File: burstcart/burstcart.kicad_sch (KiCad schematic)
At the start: 17 parts, among them J1 IEC, J2 IEC, J3 BURST, J4 PORTA, U1 27C512, U2 CD74HCT4520E, U3 6526 CIA, U4 20V8, U5 ATtiny85-20P

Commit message: remarks about changes for v1.1
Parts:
- U4: value 20V8 -> 22V10
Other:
- note added: "2-3 normally closed"
- note added: "<- VCC !!! ->"
- note added: "<- remove MUX connection, it's too fast"
- note added: "I've got CD4320 and R1 *must* be shorted, C5 *must* be removed"
- note added: "Phi2 as ciaclk works as well (at least for register r/w) - make it jumperable"
- note added: "ROM_A15 to 22, ~{CIA} to 19 - to make logic possible"
- note added: "SP/CNT are open drain, need 3.3K pullup to VCC"
- note added: "^^^ 22V10"
- note added: "closed = SW delay clock open = HW prescaler clock"
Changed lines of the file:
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@@
+    (effects (font (size 1.27 1.27)) (justify left bottom))
+  )
+  (text "SP/CNT are open drain, need 3.3K pullup to VCC" (at 174.625 156.845 0)
+    (effects (font (size 1.27 1.27)) (justify left bottom))
+  )
+  (text "<- VCC !!! ->" (at 180.975 83.82 0)
     (effects (font (size 1.27 1.27)) (justify left bottom))
   )
@@
     (effects (font (size 1.27 1.27)) (justify left bottom))
   )
+  (text "<- remove MUX connection, it's too fast" (at 189.23 114.3 0)
+    (effects (font (size 1.27 1.27)) (justify left bottom))
+  )
   (text "CC=bottom left" (at 24.765 23.495 0)
     (effects (font (size 1.27 1.27)) (justify left bottom))
   )
+  (text "I've got CD4320 and R1 *must* be shorted, C5 *must* be removed"
+    (at 160.655 36.195 0)
+    (effects (font (size 1.27 1.27)) (justify left bottom))
+  )
   (text "DELAY\nCIRCUIT" (at 170.307 59.055 0)
     (effects (font (size 1.27 1.27)) (justify left bottom))
   )
+  (text "^^^ 22V10" (at 226.06 66.04 0)
+    (effects (font (size 1.27 1.27)) (justify left bottom))
+  )
+  (text "2-3 normally closed" (at 107.315 41.91 0)
+    (effects (font (size 1.27 1.27)) (justify left bottom))
+  )
+  (text "<- VCC !!! ->" (at 165.735 101.6 0)
+    (effects (font (size 1.27 1.27)) (justify left bottom))
+  )
+  (text "<- VCC !!! ->" (at 240.665 114.3 0)
+    (effects (font (size 1.27 1.27)) (justify left bottom))
+  )
   (text "1=top right" (at 69.215 94.615 0)
     (effects (font (size 1.27 1.27)) (justify left bottom))
   )
   (text "~886 kHz" (at 170.942 44.45 0)
+    (effects (font (size 1.27 1.27)) (justify left bottom))
+  )
+  (text "closed = SW delay clock\nopen = HW prescaler clock" (at 177.8 130.81 0)
     (effects (font (size 1.27 1.27)) (justify left bottom))
   )
@@
   (text "64K:\n$0000-$7FFF = ROM C1\n$8000-$FFFF = ROM C2\n32K:\n$0000-$7FFF = ROM C1\n"
     (at 33.02 188.595 0)
+    (effects (font (size 1.27 1.27)) (justify left bottom))
+  )
+  (text "Phi2 as ciaclk works as well (at least for register r/w) - make it jumperable"
+    (at 171.45 48.26 0)
+    (effects (font (size 1.27 1.27)) (justify left bottom))
+  )
+  (text "ROM_A15 to 22, ~{CIA} to 19 - to make logic possible"
+    (at 241.3 51.435 0)
+    (effects (font (size 1.27 1.27)) (justify left bottom))
+  )
+  (text "<- VCC !!! ->" (at 214.63 113.03 0)
     (effects (font (size 1.27 1.27)) (justify left bottom))
   )
@@
       (effects (font (size 1.778 1.5113)))
     )
-    (property "Value" "20V8" (id 1) (at 208.28 72.39 0)
+    (property "Value" "22V10" (id 1) (at 208.28 72.39 0)
       (effects (font (size 1.778 1.5113)) (justify left bottom) hide)
     )
@@
       (effects (font (size 1.778 1.5113)) (justify left))
     )
-    (property "Value" "20V8" (id 1) (at 269.24 149.86 0)
+    (property "Value" "22V10" (id 1) (at 269.24 149.86 0)
       (effects (font (size 1.778 1.5113)) (justify left bottom) hide)
     )
@@
     )
     (path "/8ee1e45e-cba1-4081-b0af-4e6ecdf0aa16"
-      (reference "U4") (unit 1) (value "20V8") (footprint "Package_DIP:DIP-24_W7.62mm_Socket")
+      (reference "U4") (unit 1) (value "22V10") (footprint "Package_DIP:DIP-24_W7.62mm_Socket")
     )
     (path "/cfc3e13e-62e9-42c5-a477-ae201d8d7419"
-      (reference "U4") (unit 2) (value "20V8") (footprint "Package_DIP:DIP-24_W7.62mm_Socket")
+      (reference "U4") (unit 2) (value "22V10") (footprint "Package_DIP:DIP-24_W7.62mm_Socket")
     )
     (path "/3ae3b679-298f-4314-8545-21f8261cf41c"

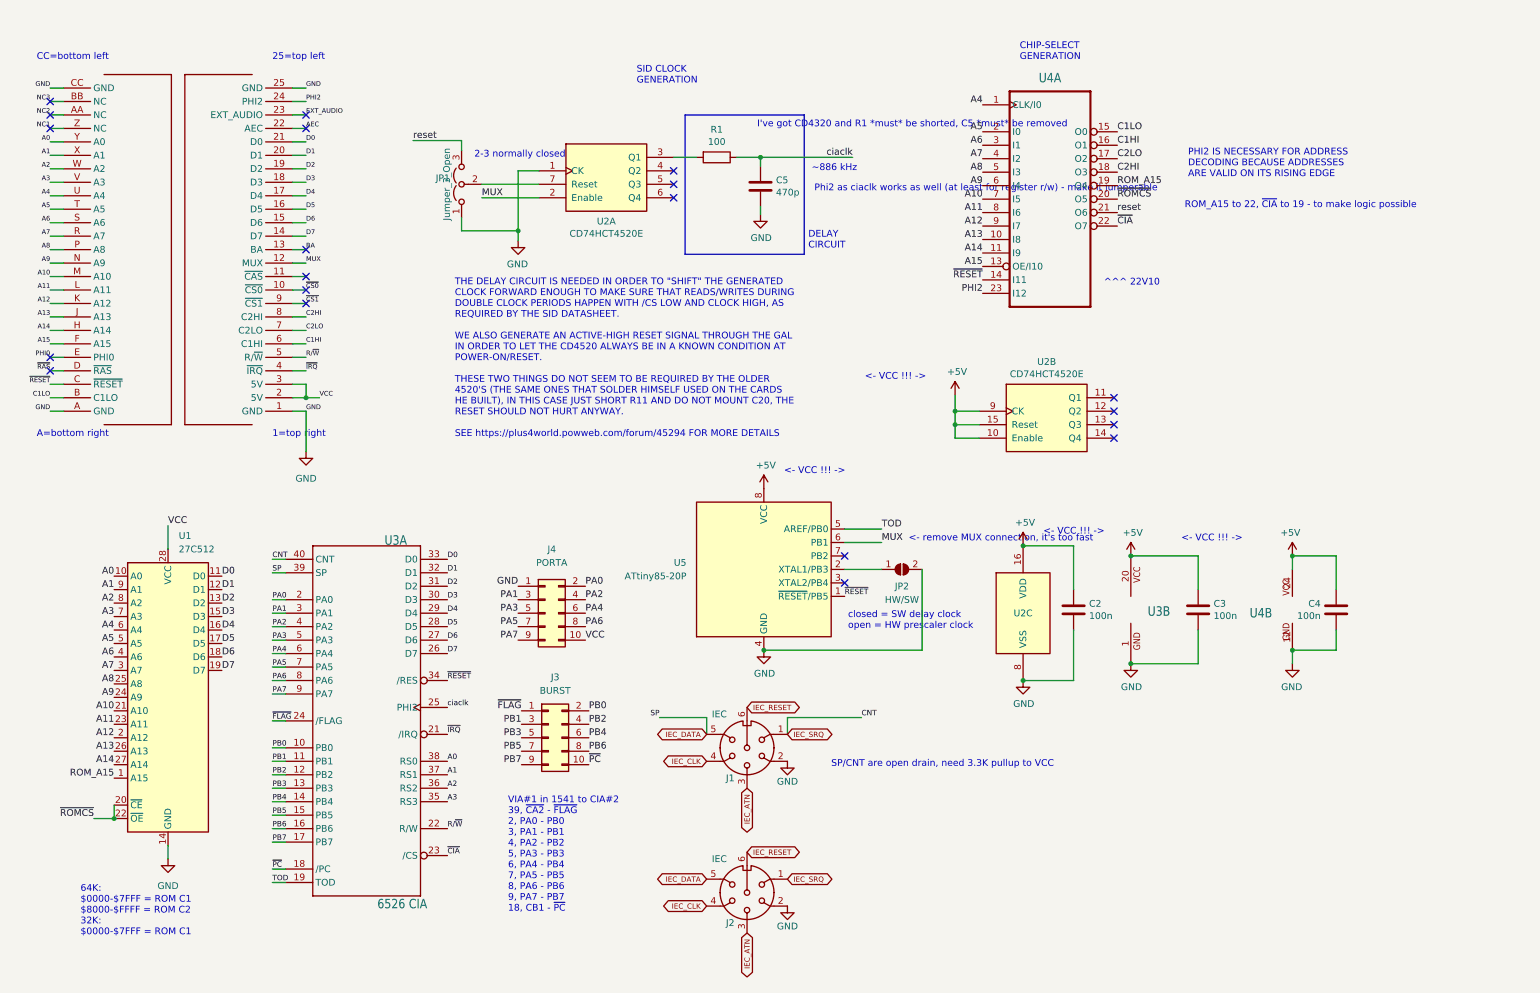
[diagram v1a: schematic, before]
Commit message: - +5V net removed, all is VCC now - /CIA is pin 19, /ROM_A15 pin 22 now - default jumper shorted to reset CD4520 - default jumper shorted to phi2 for CIACLK - GAL is 22V10 - removed MUX connection to ATTINY - pullups for SP/CNT - silkscreen texts
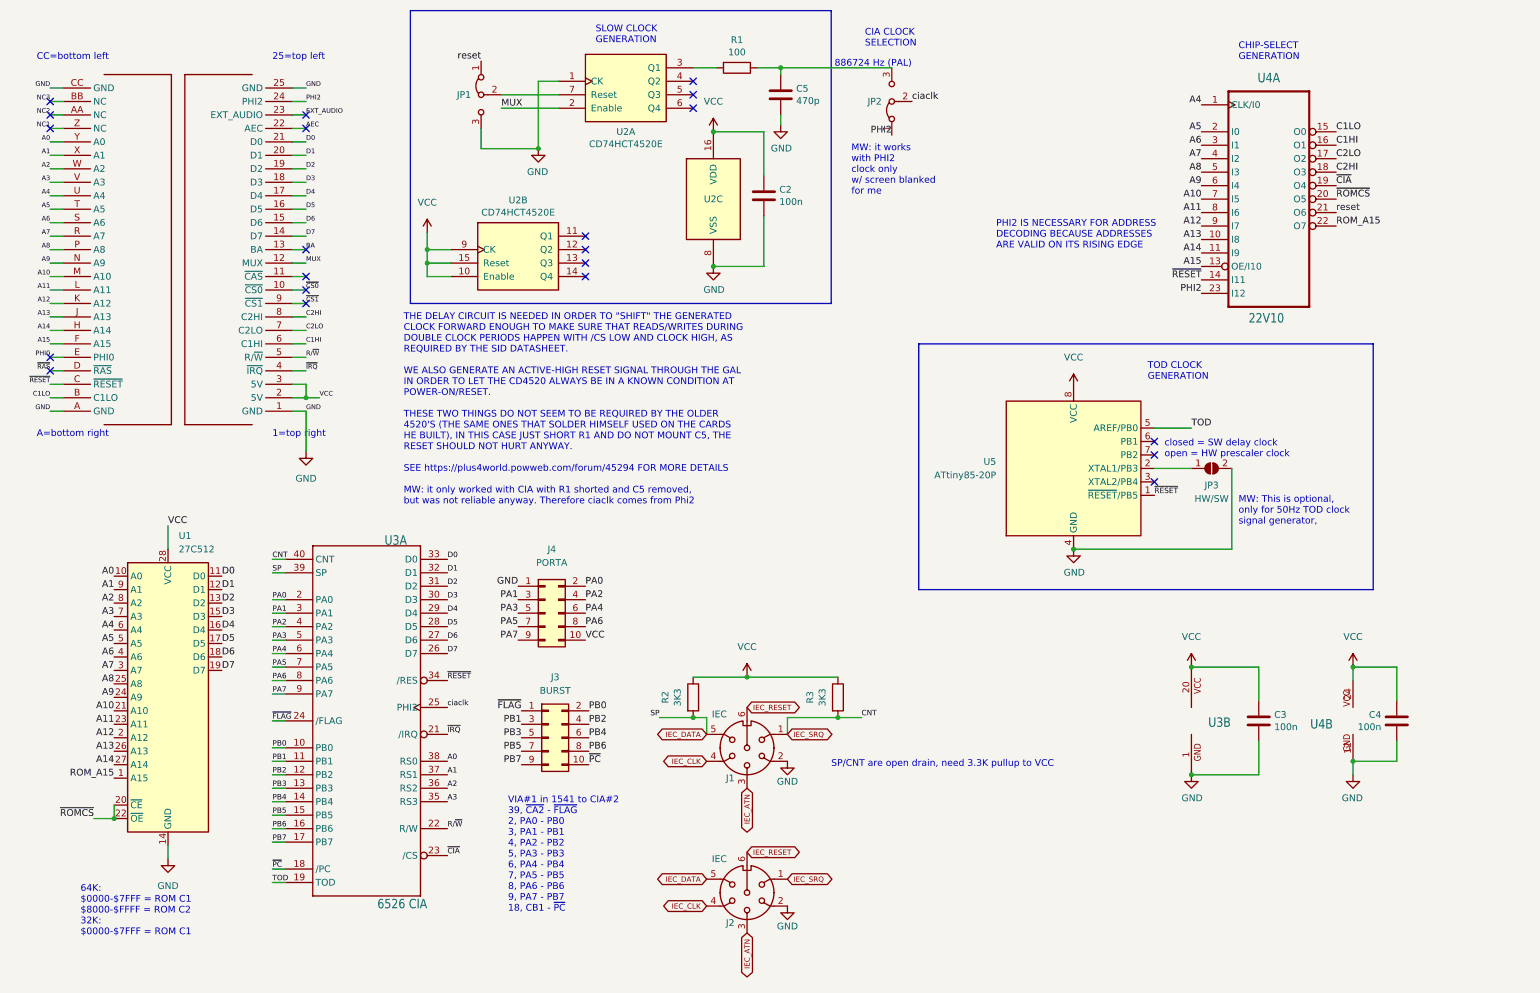
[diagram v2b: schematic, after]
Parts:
- removed JP1: Jumper_3_Open, Jumper:SolderJumper-3_P1.3mm_Open_RoundedPad1.0x1.5mm, symbol Jumper:Jumper_3_Open
- added JP1, JP2: Jumper_3_Bridged12, Jumper:SolderJumper-3_P1.3mm_Bridged2Bar12_Pad1.0x1.5mm_NumberLabels, symbol Jumper:Jumper_3_Bridged12
- added R2, R3: 3K3, Resistor_THT:R_Axial_DIN0207_L6.3mm_D2.5mm_P10.16mm_Horizontal, symbol Device:R
- renumbered JP2 to JP3
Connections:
- net +5V is gone; now on net VCC: C2.1, C3.1, C4.1, U2.10 (Enable), U2.15 (Reset), U2.16 (VDD), U2.9 (CK), U3.20 (VCC), U4.24 (VCC), U5.8 (VCC)
- net GND: now also JP1.3 (B)
- net IEC_DATA: now also R2.2
- net IEC_SRQ: now also R3.2
- net MUX: no longer U5.6 (PB1)
- net PHI2: now also JP2.1 (A)
- net ROM_A15: now also U4.22 (O7); no longer U4.19 (O4)
- net VCC: now also R2.1, R3.1
- net ciaclk: now also JP2.2 (C); no longer C5.1, R1.1
- net reset: now also JP1.1 (A)
- net ~{CIA}: now also U4.19 (O4); no longer U4.22 (O7)
- net at U2.7 (Reset): now also JP1.2 (C)
- new net: C5.1, JP2.3 (B), R1.1
- no-connect marks 20 -> 21
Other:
- note added: "886724 Hz (PAL)"
- note added: "CIA CLOCK SELECTION"
- note added: "MW: This is optional, only for 50Hz TOD clock signal generator,"
- note added: "MW: it works with PHI2 clock only w/ screen blanked for me"
- note added: "SLOW CLOCK GENERATION"
- note added: "TOD CLOCK GENERATION"
- note removed: "2-3 normally closed"
- note removed: "<- VCC !!! ->"
- note removed: "<- remove MUX connection, it's too fast"
- note removed: "DELAY CIRCUIT"
- note removed: "I've got CD4320 and R1 *must* be shorted, C5 *must* be removed"
- note removed: "Phi2 as ciaclk works as well (at least for register r/w) - make it jumperable"
- note removed: "ROM_A15 to 22, ~{CIA} to 19 - to make logic possible"
- note removed: "SID CLOCK GENERATION"
- note removed: "^^^ 22V10"
- note removed: "~886 kHz"
- moved on the sheet: C2, C3, C4, C5, JP3, R1, U2A, U2B, U2C, U3B, U4A, U4B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
